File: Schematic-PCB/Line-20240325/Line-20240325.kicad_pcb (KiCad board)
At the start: 2 copper layers, 195 x 168 mm, 172 parts, among them J1 Conn_01x02_Pin, J2 Conn_01x04_Pin, J3 Conn_01x06_Pin, SW1 SW_Push, U33 ATmega2560-16A, Y1 16MHz

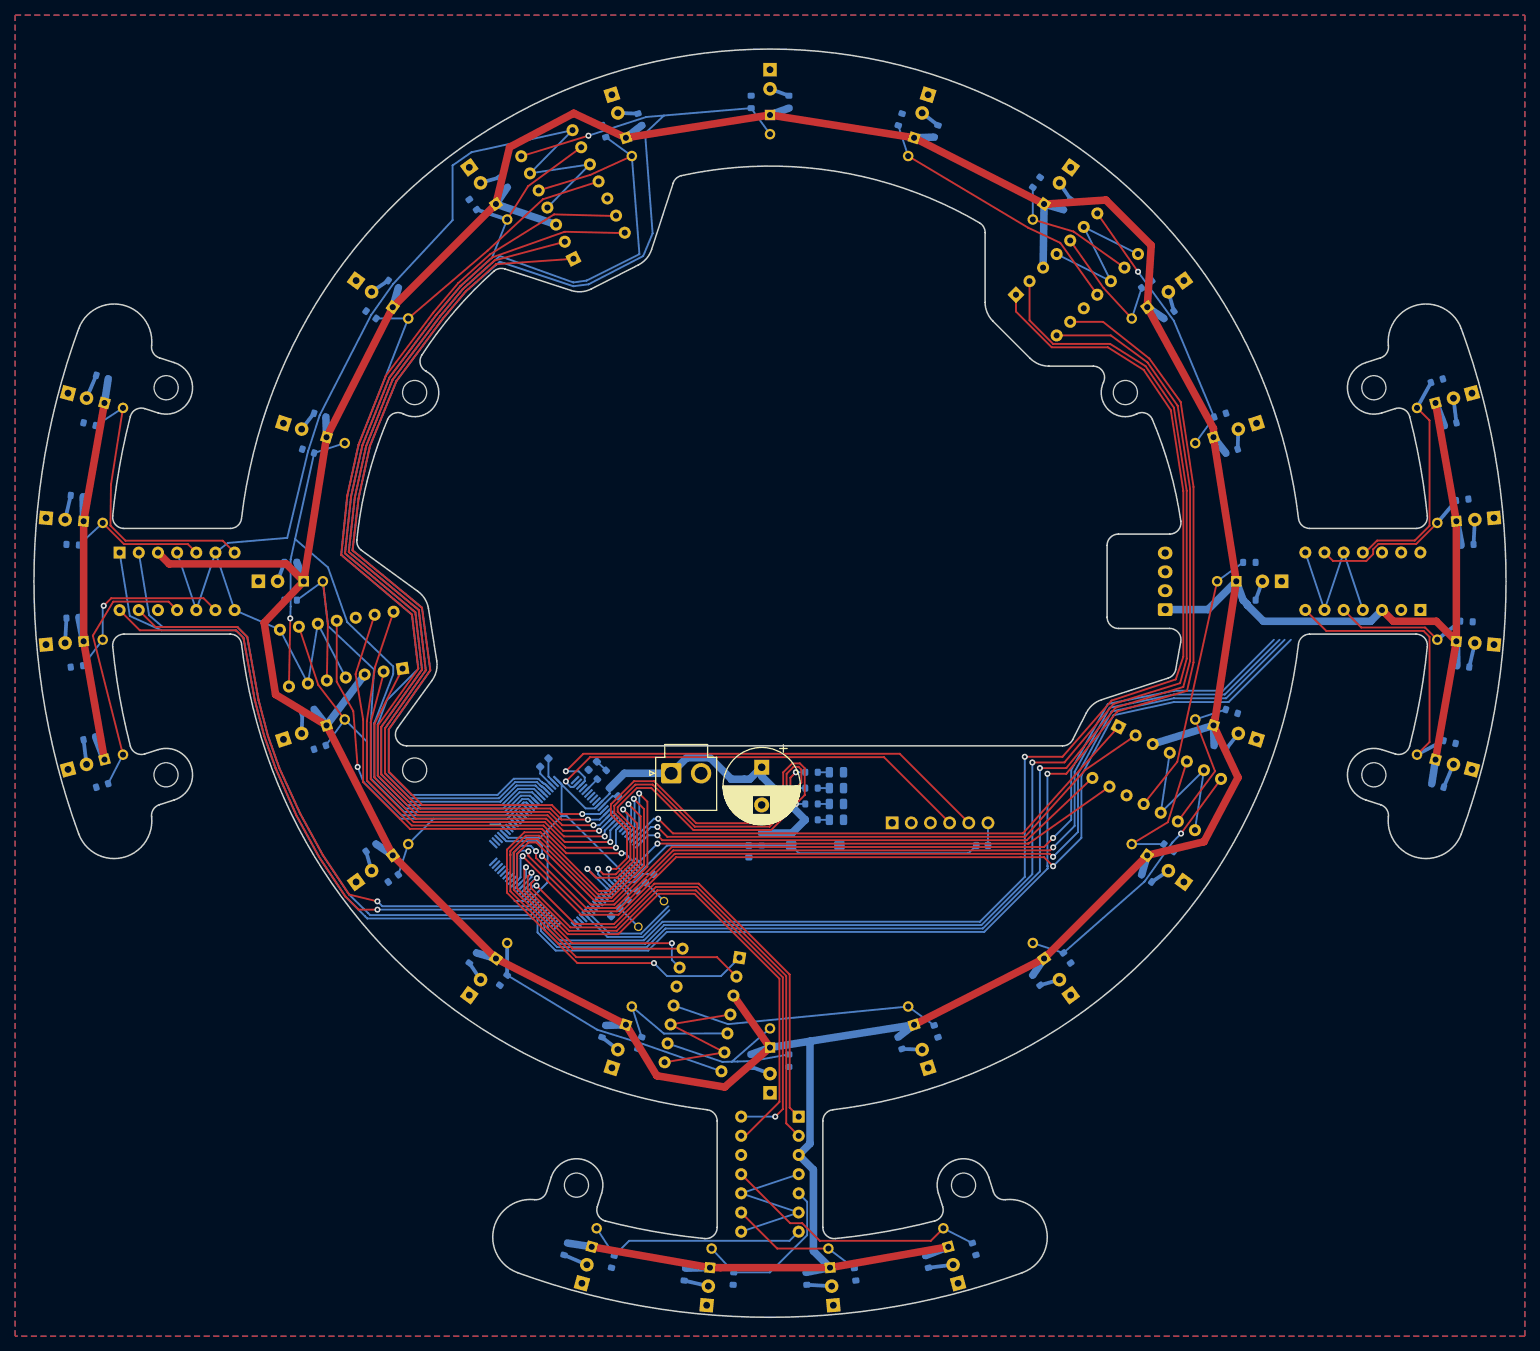
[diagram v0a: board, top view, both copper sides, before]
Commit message: ライン基板の配線を進めた
line_thresholdとかをちょろっと繋いだ
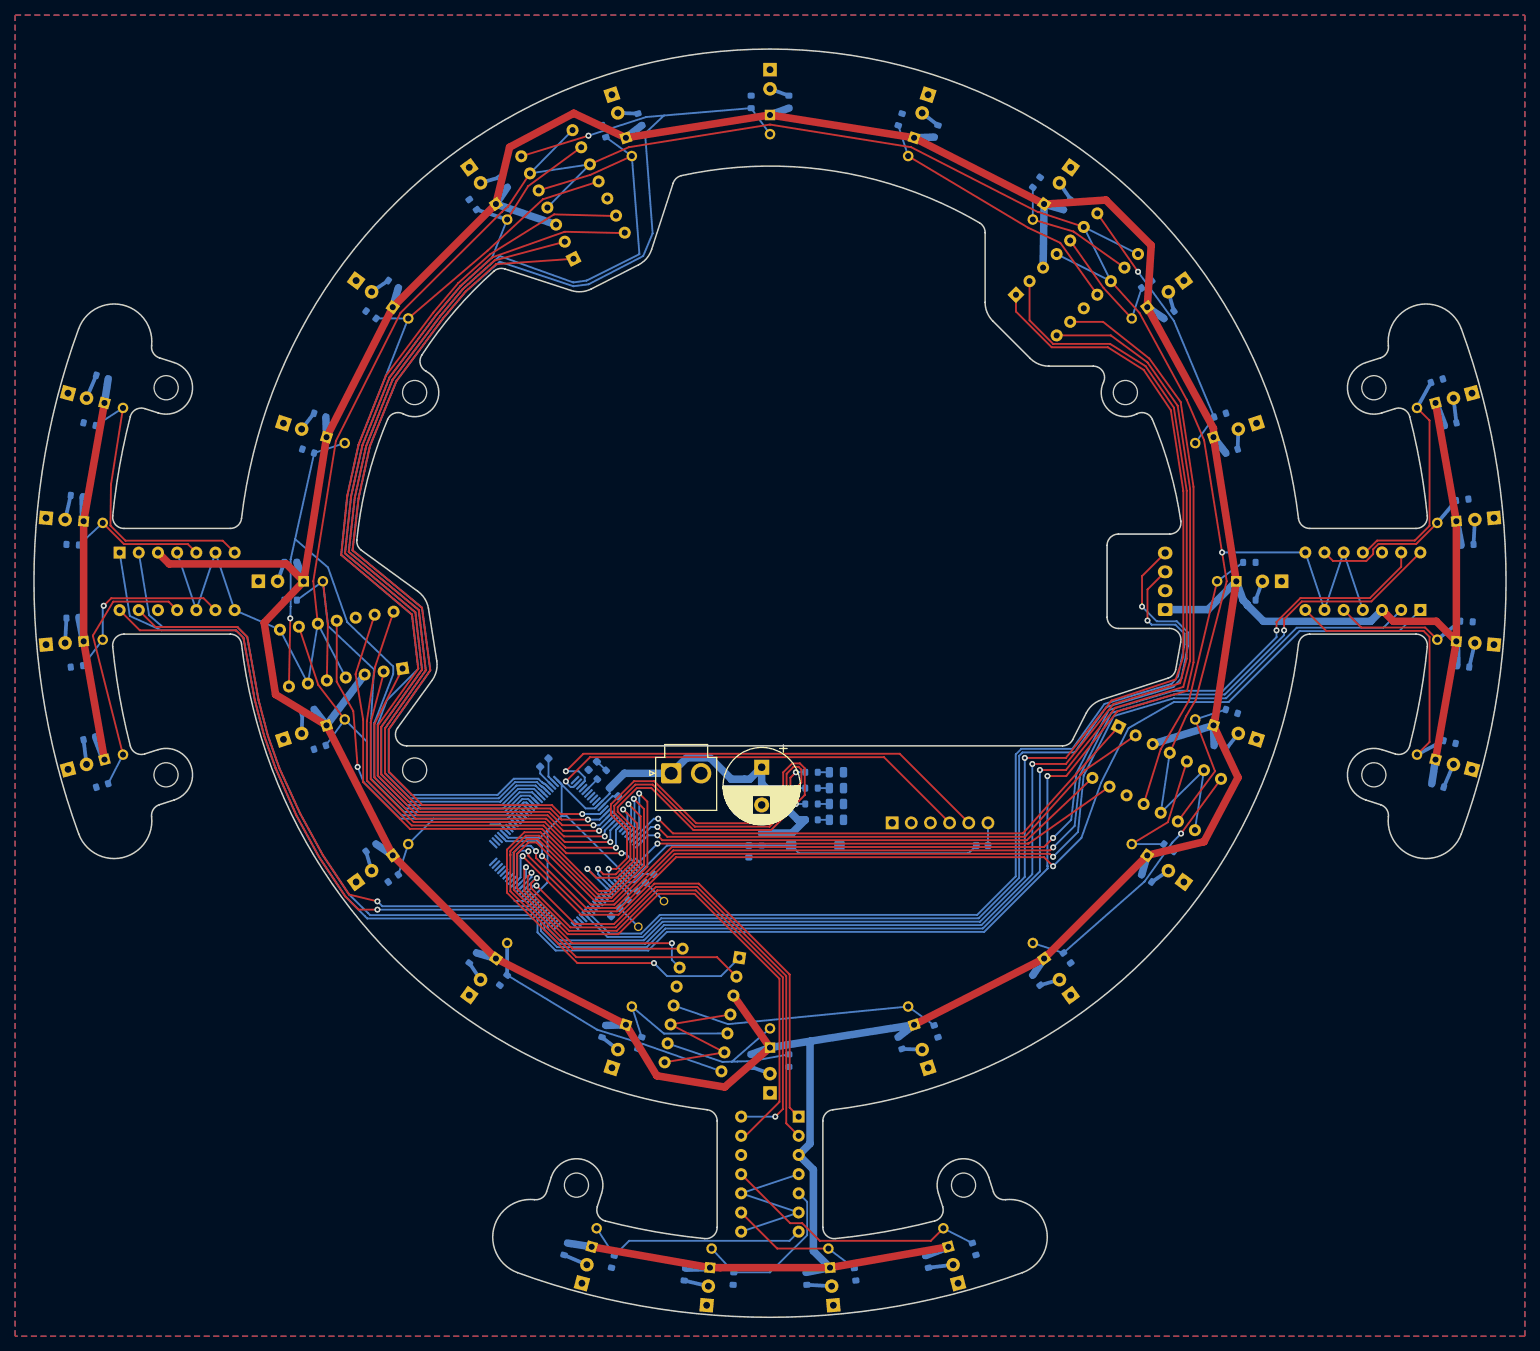
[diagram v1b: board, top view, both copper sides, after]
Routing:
- net LineThreshold: track 283.3 -> 417.1 mm, vias 0 -> 1
- net Line-MD-Main=RX_5V: track 13.7 -> 125.7 mm, vias 0 -> 1
- net Line-MD-Main=TX_5V: track 13.2 -> 121.5 mm, vias 0 -> 1
- net Line31: track 129.2 -> 153.0 mm, vias 2 -> 3
- net Line32: track 126.3 -> 149.3 mm, vias 2 -> 3
- net Line30: track 130.1 -> 146.3 mm
- net Line29: track 130.9 -> 147.0 mm
- net +5V: track 873.6 -> 874.1 mm

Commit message: ライン
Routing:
- net LineThreshold: track 417.1 -> 498.7 mm, vias 1 -> 2
- net Line20: track 169.1 -> 169.7 mm
- net Line19: track 168.1 -> 168.6 mm

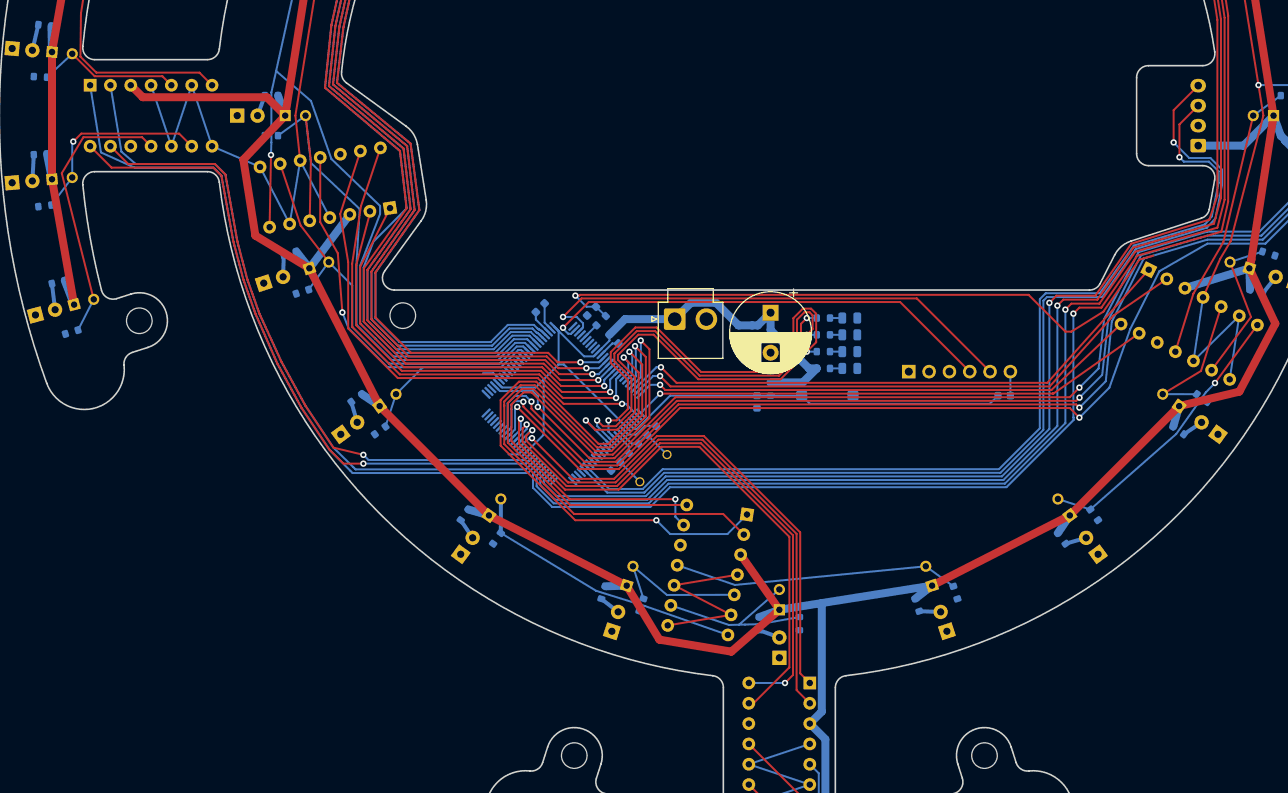
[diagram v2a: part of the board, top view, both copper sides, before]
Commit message: ラインの配線を進めた
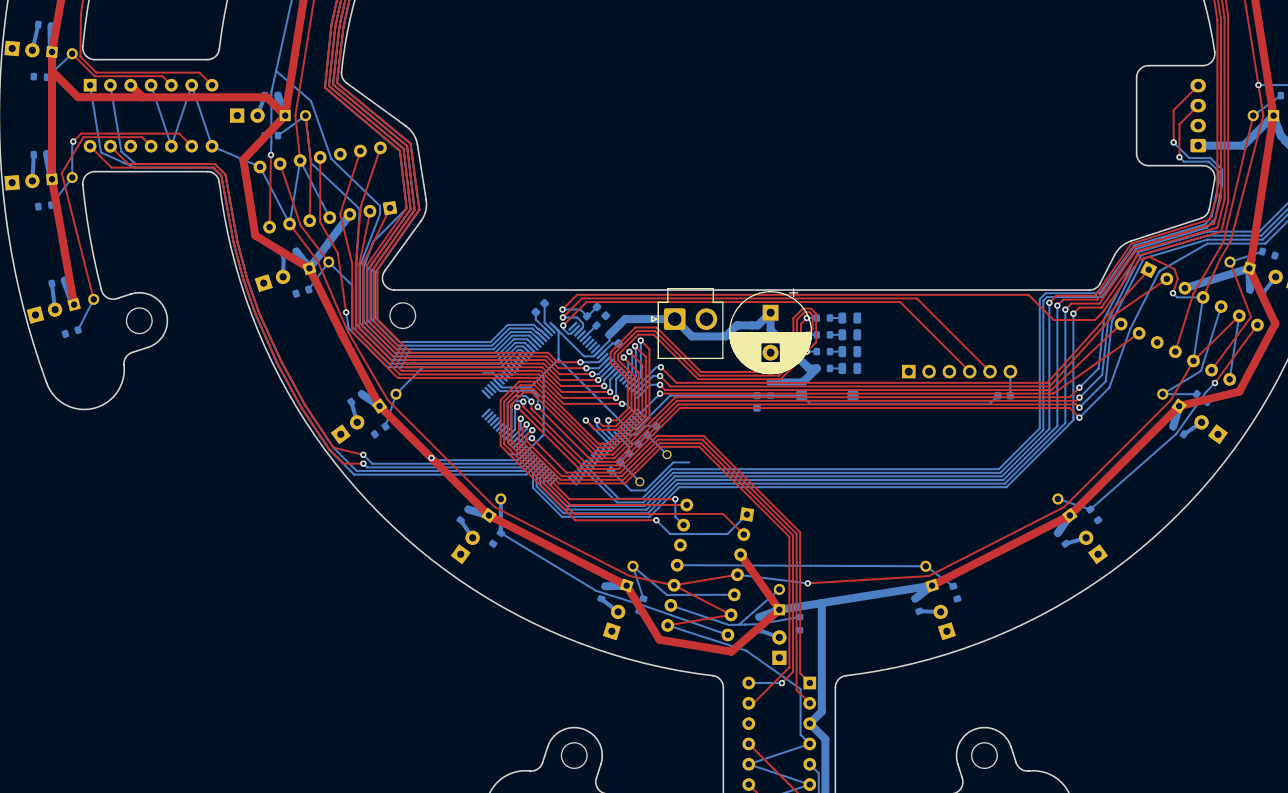
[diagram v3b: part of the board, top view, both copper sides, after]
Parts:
- moved C10 1.23 mm to (-22.2, 24.5), turned to -45 degrees
- moved R72 1.17 mm to (-23.4, 25.7), turned to 135 degrees
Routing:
- net LineThreshold: track 498.7 -> 672.9 mm, vias 2 -> 4
- net +5V: track 874.1 -> 899.1 mm, vias 0 -> 1
- net GND: track 15.5 -> 27.8 mm
- net Line-MD-Main=RX_5V: track 125.7 -> 126.7 mm
- net Line20: track 169.7 -> 170.8 mm
- net Line19: track 168.6 -> 169.6 mm
- net Line18: track 175.9 -> 177.0 mm
- net Line17: track 172.9 -> 174.0 mm
- net Line-MD-Main=TX_5V: track 121.5 -> 122.6 mm
- net Line27: track 71.6 -> 70.7 mm
- net Line25: track 64.1 -> 63.5 mm
- net Line28: track 72.5 -> 71.8 mm
- net Line26: track 69.2 -> 68.5 mm
- net Raw12: track 35.9 -> 35.3 mm

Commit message: ライン基板を完成させた
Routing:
- net Raw5: track 97.3 -> 99.2 mm, vias 1 -> 2
- net Raw26: track 22.1 -> 23.7 mm
- net GND: vias 0 -> 71

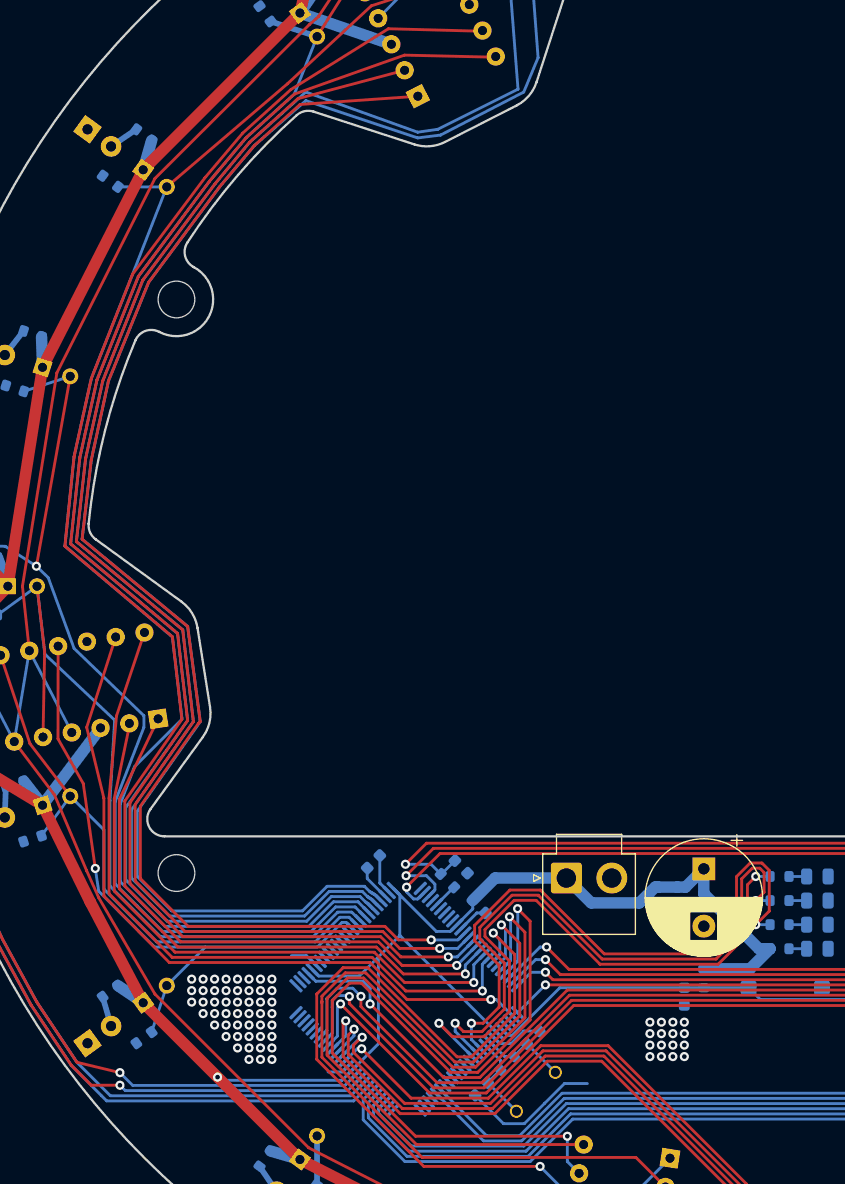
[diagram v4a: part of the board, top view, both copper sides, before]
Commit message: ラインセンサの発注用ファイルなどを出力
進捗生んだ。
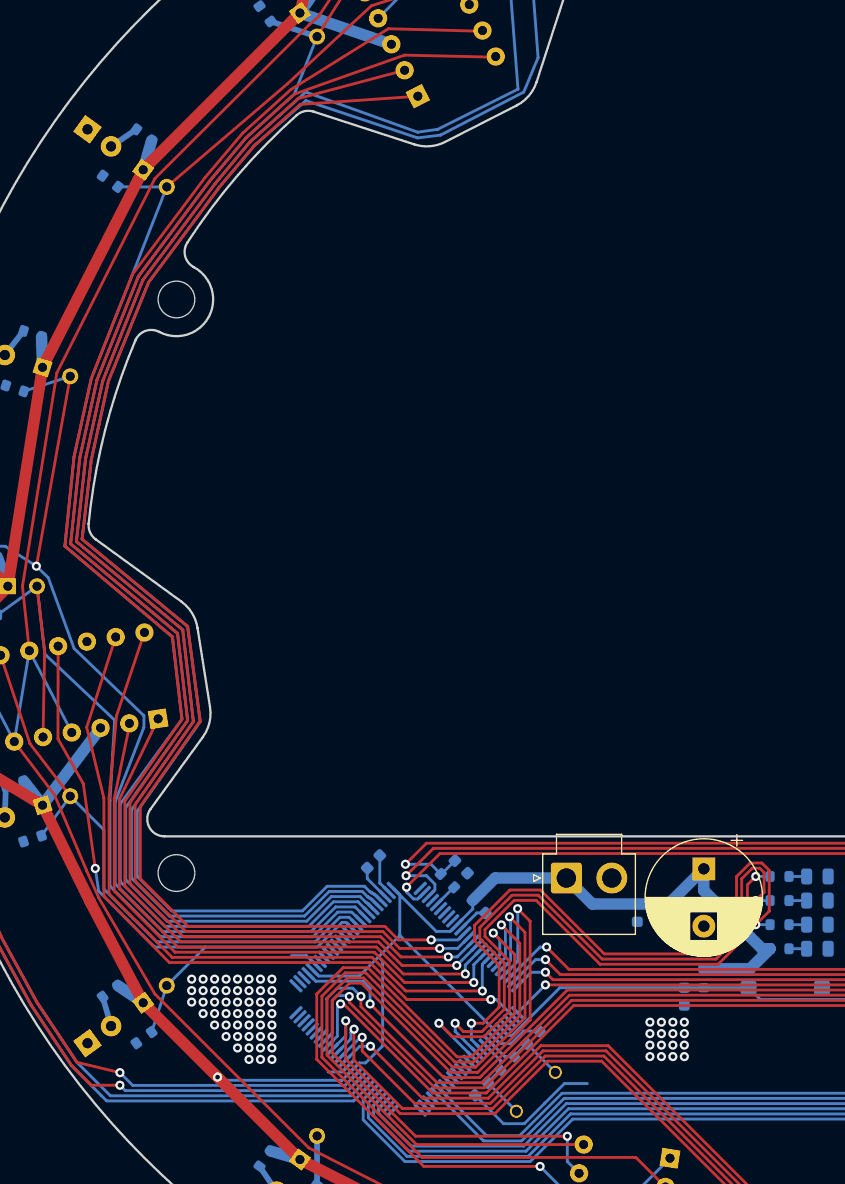
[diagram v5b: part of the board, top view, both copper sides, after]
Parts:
- moved C2 2.33 mm to (-6.90, 28.5)
- moved C3 2.33 mm to (-5.20, 28.5)
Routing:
- net Line26: track 68.5 -> 67.4 mm
- net +5V: track 899.1 -> 899.7 mm
